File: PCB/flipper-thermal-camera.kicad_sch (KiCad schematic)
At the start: 9 parts, among them J1 Conn_01x08, J2 Conn_01x10, U1 MLX90640ESF-BAB-000-SP, U2 XC6206PxxxMR

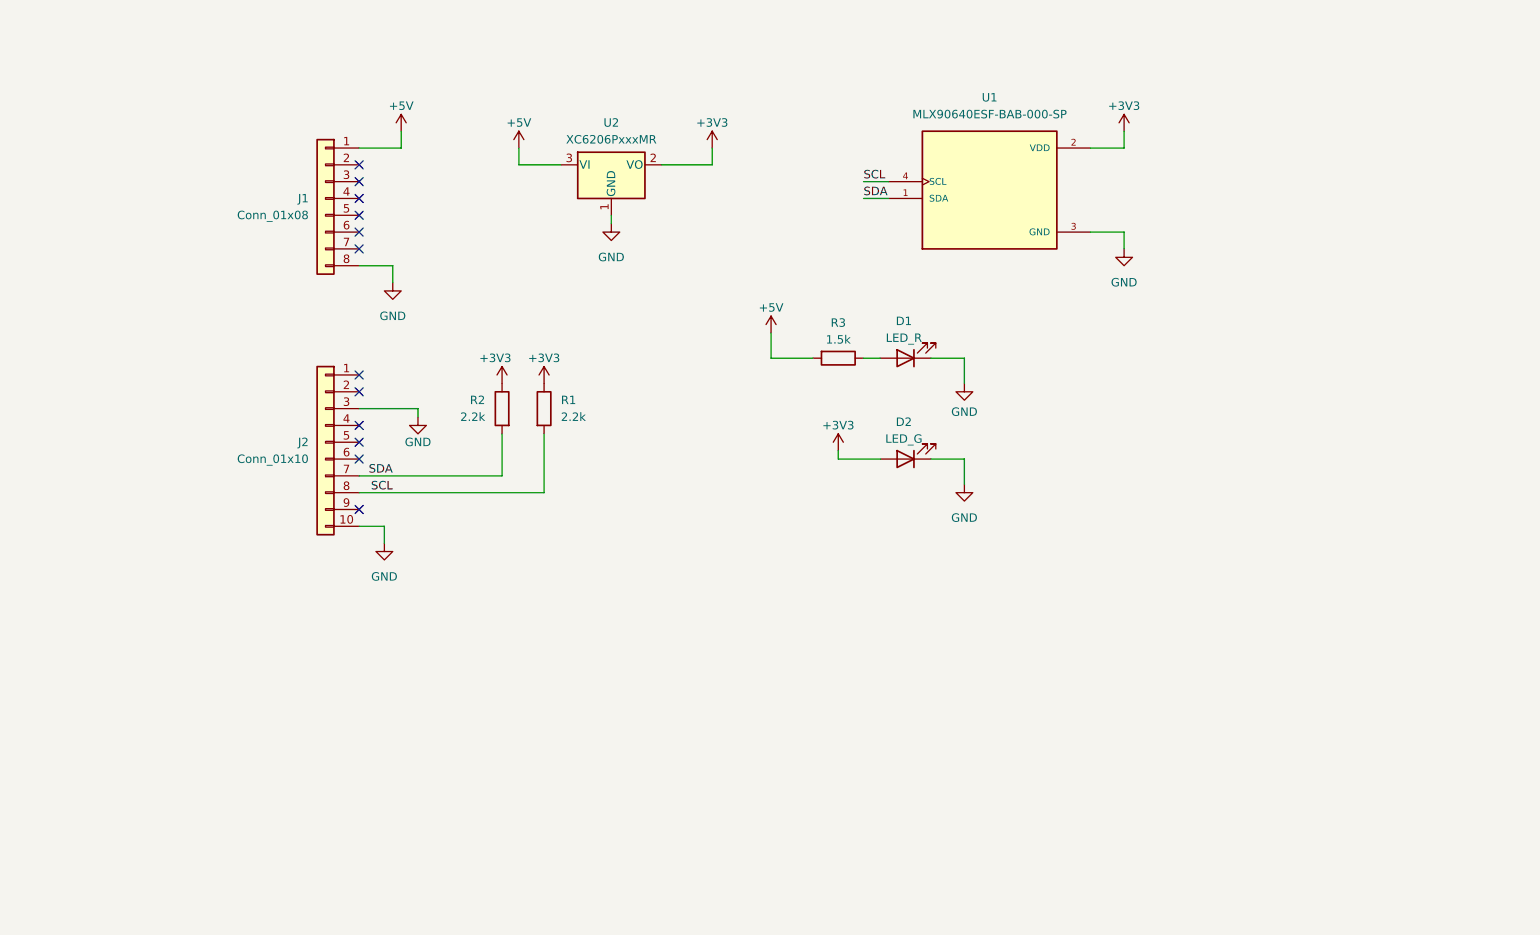
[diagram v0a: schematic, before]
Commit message: add IMU, temp sensor, and light sensor + capacitors
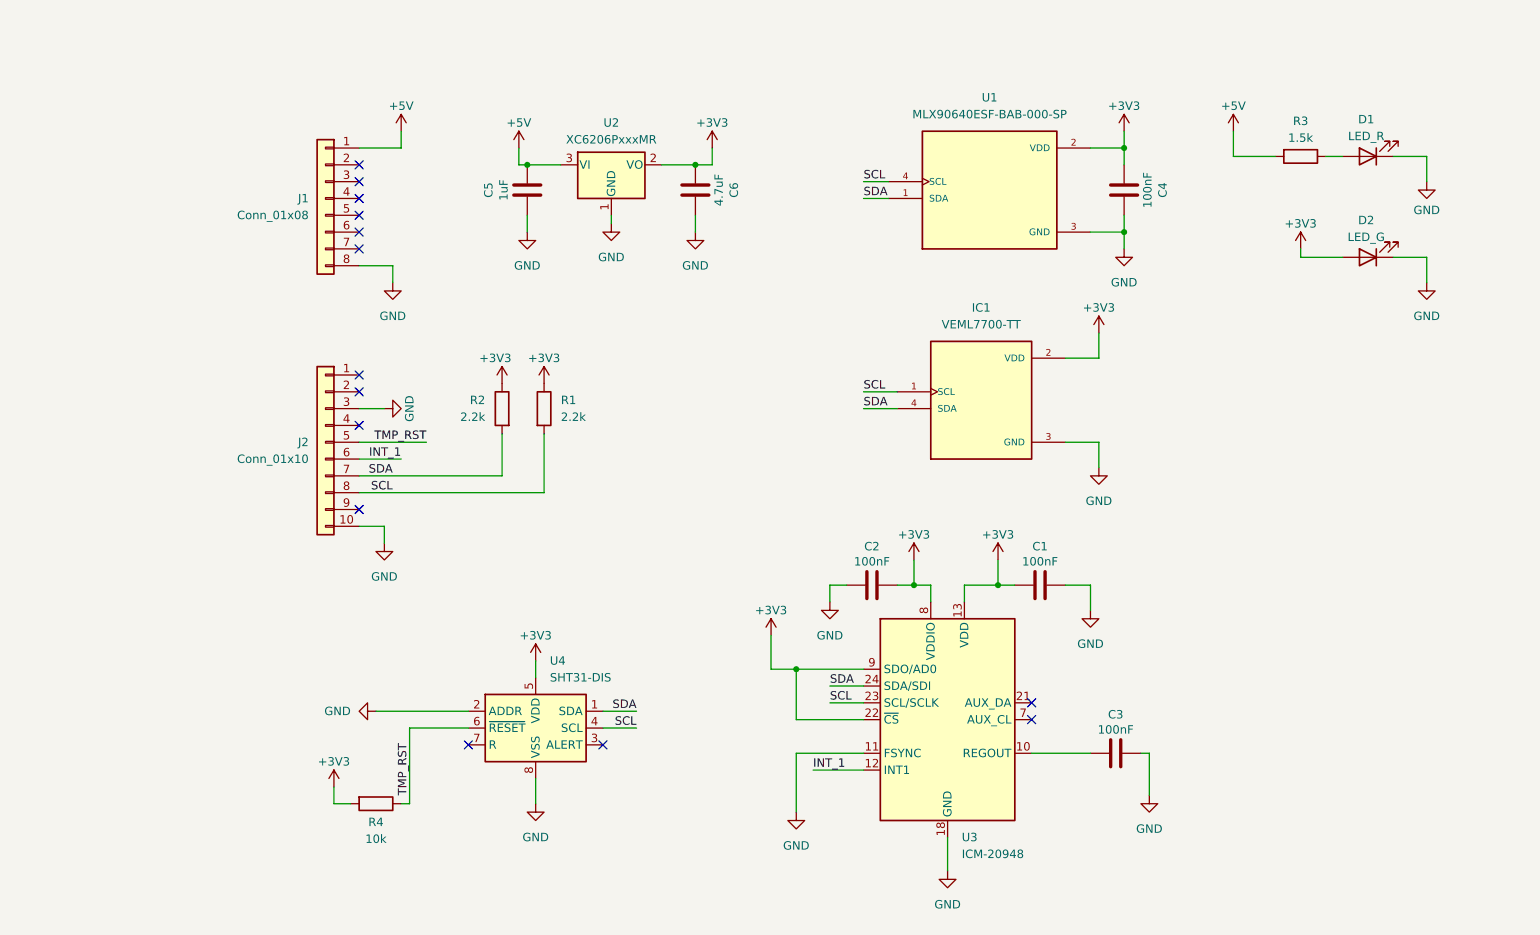
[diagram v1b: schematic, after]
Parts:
- added C1, C2, C3, C4: 100nF, Capacitor_SMD:C_0805_2012Metric, symbol Device:C
- added C5: 1uF, Capacitor_SMD:C_0805_2012Metric, symbol Device:C
- added C6: 4.7uF, Capacitor_SMD:C_0805_2012Metric, symbol Device:C
- added IC1: VEML7700-TT, Components:XDCR_VEML7700-TT, symbol VEML7700-TT:VEML7700-TT
- added R4: 10k, Resistor_SMD:R_0805_2012Metric, symbol Device:R
- added U3: ICM-20948, Sensor_Motion:InvenSense_QFN-24_3x3mm_P0.4mm, symbol Sensor_Motion:ICM-20948
- added U4: SHT31-DIS, Sensor_Humidity:Sensirion_DFN-8-1EP_2.5x2.5mm_P0.5mm_EP1.1x1.7mm, symbol Sensor_Humidity:SHT31-DIS
- D1, D2: footprint (none) -> LED_SMD:LED_0805_2012Metric
- J1: footprint (none) -> Connector_PinHeader_2.54mm:PinHeader_1x08_P2.54mm_Vertical
- J2: footprint (none) -> Connector_PinHeader_2.54mm:PinHeader_1x10_P2.54mm_Vertical
- R1, R2, R3: footprint (none) -> Resistor_SMD:R_0805_2012Metric
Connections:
- net +3V3: now also C1.1, C2.2, C4.1, C6.2, IC1.2 (VDD), R4.2, U3.13 (VDD), U3.22 (~{CS}), U3.8 (VDDIO), U3.9 (SDO/AD0), U4.5 (VDD)
- net +5V: now also C5.2
- net GND: now also C1.2, C2.1, C3.2, C4.2, C5.1, C6.1, IC1.3 (GND), U3.11 (FSYNC), U3.18 (GND), U3.20 (GND), U4.2 (ADDR), U4.8 (VSS), U4.9 (VSS)
- net SCL: now also IC1.1 (SCL), U3.23 (SCL/SCLK), U4.4 (SCL)
- net SDA: now also IC1.4 (SDA), U3.24 (SDA/SDI), U4.1 (SDA)
- net TMP_RST: now reaches J2.5 (Pin_5)
- net TMP_RST: now also R4.1, U4.6 (~{RESET})
- net INT_1: now reaches J2.6 (Pin_6)
- net INT_1: now also U3.12 (INT1)
- new net: C3.1, U3.10 (REGOUT)
- no-connect marks 12 -> 14
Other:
- moved on the sheet: D1, D2, R3

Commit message: finish schematic
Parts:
- J1: footprint Connector_PinHeader_2.54mm:PinHeader_1x08_P2.54mm_Vertical -> Connector_PinHeader_2.54mm:PinHeader_1x08_P2.54mm_Horizontal
- J2: footprint Connector_PinHeader_2.54mm:PinHeader_1x10_P2.54mm_Vertical -> Connector_PinHeader_2.54mm:PinHeader_1x10_P2.54mm_Horizontal
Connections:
- net +5V: now also J1.8 (Pin_8); no longer J1.1 (Pin_1)
- net GND: now also J1.1 (Pin_1), J2.1 (Pin_1), J2.8 (Pin_8); no longer J1.8 (Pin_8), J2.10 (Pin_10), J2.3 (Pin_3)
- net INT_1: now also J2.5 (Pin_5); no longer J2.6 (Pin_6)
- net SCL: now also J2.3 (Pin_3); no longer J2.8 (Pin_8)
- net SDA: now also J2.4 (Pin_4); no longer J2.7 (Pin_7)
- net TMP_RST: now also J2.6 (Pin_6); no longer J2.5 (Pin_5)
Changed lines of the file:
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@@
 	)
 	(symbol
-		(lib_id "Connector_Generic:Conn_01x08")
-		(at 62.23 48.26 0)
-		(mirror y)
-		(unit 1)
-		(body_style 1)
-		(exclude_from_sim no)
-		(in_bom yes)
-		(on_board yes)
-		(in_pos_files yes)
-		(dnp no)
-		(fields_autoplaced yes)
-		(property "Reference" "J1"
-			(at 59.69 48.2599 0)
-			(show_name no)
-			(do_not_autoplace no)
-			(effects
-				(font
-					(size 1.27 1.27)
-				)
-				(justify left)
-			)
-		)
-		(property "Value" "Conn_01x08"
-			(at 59.69 50.7999 0)
-			(show_name no)
-			(do_not_autoplace no)
-			(effects
-				(font
-					(size 1.27 1.27)
-				)
-				(justify left)
-			)
-		)
-		(property "Footprint" "Connector_PinHeader_2.54mm:PinHeader_1x08_P2.54mm_Vertical"
-			(at 62.23 48.26 0)
-			(hide yes)
-			(show_name no)
-			(do_not_autoplace no)
-			(effects
-				(font
-					(size 1.27 1.27)
-				)
-			)
-		)
-		(property "Datasheet" ""
-			(at 62.23 48.26 0)
-			(hide yes)
-			(show_name no)
-			(do_not_autoplace no)
-			(effects
-				(font
-					(size 1.27 1.27)
-				)
-			)
-		)
-		(property "Description" "Generic connector, single row, 01x08, script generated (kicad-library-utils/schlib/autogen/connector/)"
-			(at 62.23 48.26 0)
-			(hide yes)
-			(show_name no)
-			(do_not_autoplace no)
-			(effects
-				(font
-					(size 1.27 1.27)
-				)
-			)
-		)
-		(pin "1"
-		)
-		(pin "3"
-		)
-		(pin "4"
-		)
-		(pin "5"
-		)
-		(pin "6"
-		)
-		(pin "8"
-		)
-		(pin "2"
-		)
-		(pin "7"
-		)
-		(instances
-			(project "flipper-thermal-camera"
-				(path "/20fef62b-baec-4471-9252-b8b8b3debd81"
-					(reference "J1")
-					(unit 1)
-				)
-			)
-		)
-	)
-	(symbol
 		(lib_id "Regulator_Linear:XC6206PxxxMR")
 		(at 105.41 43.18 0)
@@
 	)
 	(symbol
+		(lib_id "Connector_Generic:Conn_01x10")
+		(at 62.23 87.63 180)
+		(unit 1)
+		(body_style 1)
+		(exclude_from_sim no)
+		(in_bom yes)
+		(on_board yes)
+		(in_pos_files yes)
+		(dnp no)
+		(property "Reference" "J2"
+			(at 62.23 68.58 0)
+			(show_name no)
+			(do_not_autoplace no)
+			(effects
+				(font
+					(size 1.27 1.27)
+				)
+			)
+		)
+		(property "Value" "Conn_01x10"
+			(at 62.23 71.12 0)
+			(show_name no)
+			(do_not_autoplace no)
+			(effects
+				(font
+					(size 1.27 1.27)
+				)
+			)
+		)
+		(property "Footprint" "Connector_PinHeader_2.54mm:PinHeader_1x10_P2.54mm_Horizontal"
+			(at 62.23 87.63 0)
+			(hide yes)
+			(show_name no)
+			(do_not_autoplace no)
+			(effects
+				(font
+					(size 1.27 1.27)
+				)
+			)
+		)
+		(property "Datasheet" ""
+			(at 62.23 87.63 0)
+			(hide yes)
+			(show_name no)
+			(do_not_autoplace no)
+			(effects
+				(font
+					(size 1.27 1.27)
+				)
+			)
+		)
+		(property "Description" "Generic connector, single row, 01x10, script generated (kicad-library-utils/schlib/autogen/connector/)"
+			(at 62.23 87.63 0)
+			(hide yes)
+			(show_name no)
+			(do_not_autoplace no)
+			(effects
+				(font
+					(size 1.27 1.27)
+				)
+			)
+		)
+		(pin "9"
+		)
+		(pin "2"
+		)
+		(pin "7"
+		)
+		(pin "10"
+		)
+		(pin "3"
+		)
+		(pin "5"
+		)
+		(pin "4"
+		)
+		(pin "1"
+		)
+		(pin "6"
+		)
+		(pin "8"
+		)
+		(instances
+			(project "flipper-thermal-camera"
+				(path "/20fef62b-baec-4471-9252-b8b8b3debd81"
+					(reference "J2")
+					(unit 1)
+				)
+			)
+		)
+	)
+	(symbol
 		(lib_id "Device:R")
 		(at 69.85 139.7 270)
@@
 	)
 	(symbol
+		(lib_id "Connector_Generic:Conn_01x08")
+		(at 62.23 50.8 180)
+		(unit 1)
+		(body_style 1)
+		(exclude_from_sim no)
+		(in_bom yes)
+		(on_board yes)
+		(in_pos_files yes)
+		(dnp no)
+		(property "Reference" "J1"
+			(at 62.23 34.29 0)
+			(show_name no)
+			(do_not_autoplace no)
+			(effects
+				(font
+					(size 1.27 1.27)
+				)
+			)
+		)
+		(property "Value" "Conn_01x08"
+			(at 62.23 36.83 0)
+			(show_name no)
+			(do_not_autoplace no)
+			(effects
+				(font
+					(size 1.27 1.27)
+				)
+			)
+		)
+		(property "Footprint" "Connector_PinHeader_2.54mm:PinHeader_1x08_P2.54mm_Horizontal"
+			(at 62.23 50.8 0)
+			(hide yes)
+			(show_name no)
+			(do_not_autoplace no)
+			(effects
+				(font
+					(size 1.27 1.27)
+				)
+			)
+		)
+		(property "Datasheet" ""
+			(at 62.23 50.8 0)
+			(hide yes)
+			(show_name no)
+			(do_not_autoplace no)
+			(effects
+				(font
+					(size 1.27 1.27)
+				)
+			)
+		)
+		(property "Description" "Generic connector, single row, 01x08, script generated (kicad-library-utils/schlib/autogen/connector/)"
+			(at 62.23 50.8 0)
+			(hide yes)
+			(show_name no)
+			(do_not_autoplace no)
+			(effects
+				(font
+					(size 1.27 1.27)
+				)
+			)
+		)
+		(pin "1"
+		)
+		(pin "3"
+		)
+		(pin "4"
+		)
+		(pin "5"
+		)
+		(pin "6"
+		)
+		(pin "8"
+		)
+		(pin "2"
+		)
+		(pin "7"
+		)
+		(instances
+			(project "flipper-thermal-camera"
+				(path "/20fef62b-baec-4471-9252-b8b8b3debd81"
+					(reference "J1")
+					(unit 1)
+				)
+			)
+		)
+	)
+	(symbol
 		(lib_id "power:GND")
 		(at 105.41 52.07 0)
@@
 					(unit 1)
 				)
-			)
-		)
-	)
-	(symbol
-		(lib_id "Connector_Generic:Conn_01x10")
-		(at 62.23 85.09 0)
-		(mirror y)
-		(unit 1)
-		(body_style 1)
-		(exclude_from_sim no)
-		(in_bom yes)
-		(on_board yes)
-		(in_pos_files yes)
-		(dnp no)
-		(fields_autoplaced yes)
-		(property "Reference" "J2"
-			(at 59.69 85.0899 0)
-			(show_name no)
-			(do_not_autoplace no)
-			(effects
-				(font
-					(size 1.27 1.27)
-				)
-				(justify left)
-			)
-		)
-		(property "Value" "Conn_01x10"
-			(at 59.69 87.6299 0)
-			(show_name no)
-			(do_not_autoplace no)
-			(effects
-				(font
-					(size 1.27 1.27)
-				)
-				(justify left)
-			)
-		)
-		(property "Footprint" "Connector_PinHeader_2.54mm:PinHeader_1x10_P2.54mm_Vertical"
-			(at 62.23 85.09 0)
-			(hide yes)
-			(show_name no)
-			(do_not_autoplace no)
-			(effects
-				(font
-					(size 1.27 1.27)
-				)
-			)
-		)
-		(property "Datasheet" ""
-			(at 62.23 85.09 0)
-			(hide yes)
-			(show_name no)
-			(do_not_autoplace no)
-			(effects
-				(font
-					(size 1.27 1.27)
-				)
-			)
-		)
-		(property "Description" "Generic connector, single row, 01x10, script generated (kicad-library-utils/schlib/autogen/connector/)"
-			(at 62.23 85.09 0)
-			(hide yes)
-			(show_name no)
-			(do_not_autoplace no)
-			(effects
-				(font
-					(size 1.27 1.27)
-				)
-			)
-		)
-		(pin "9"
-		)
-		(pin "2"
-		)
-		(pin "7"
-		)
-		(pin "10"
-		)
-		(pin "3"
-		)
-		(pin "5"
-		)
-		(pin "4"
-		)
-		(pin "1"
-		)
-		(pin "6"
-		)
-		(pin "8"
-		)
-		(instances
-			(project "flipper-thermal-camera"
-				(path "/20fef62b-baec-4471-9252-b8b8b3debd81"
-					(reference "J2")
-					(unit 1)
-				)

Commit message: finish routing pcb
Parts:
- removed J1: Conn_01x08, Connector_PinHeader_2.54mm:PinHeader_1x08_P2.54mm_Horizontal, symbol Connector_Generic:Conn_01x08
- removed J2: Conn_01x10, Connector_PinHeader_2.54mm:PinHeader_1x10_P2.54mm_Horizontal, symbol Connector_Generic:Conn_01x10
- added A1: Flipper_Zero, Module:Flipper_Zero_Angled, symbol MCU_Module:Flipper_Zero
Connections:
- net +5V: now also A1.1 (5V)
- net GND: now also A1.11 (GND), A1.18 (GND), A1.8 (GND)
- net INT_1: now also A1.14 (USART1.RX)
- net SCL: now also A1.16 (I2C3.SCL)
- net SDA: now also A1.15 (I2C3.SDA)
- net TMP_RST: now also A1.13 (USART1.TX)
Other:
- moved on the sheet: R4, U4

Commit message: add testpoints
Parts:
- added SDA1, TP3, TP4: GND, TestPoint:TestPoint_Pad_D2.0mm, symbol Connector:TestPoint
- added TP1: 3V3, TestPoint:TestPoint_Pad_D2.0mm, symbol Connector:TestPoint
- added TP2: 5V, TestPoint:TestPoint_Pad_D2.0mm, symbol Connector:TestPoint
- added TP5: SCL, TestPoint:TestPoint_Pad_D2.0mm, symbol Connector:TestPoint
- added TP6: TMP_SENS_RST, TestPoint:TestPoint_Pad_D2.0mm, symbol Connector:TestPoint
- added TP7: INT_ICM, TestPoint:TestPoint_Pad_D2.0mm, symbol Connector:TestPoint
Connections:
- net +3V3: now also TP1.1
- net +5V: now also TP2.1
- net GND: now also TP3.1, TP4.1
- net INT_1: now also TP7.1
- net SCL: now also TP5.1
- net SDA: now also SDA1.1
- net TMP_RST: now also TP6.1

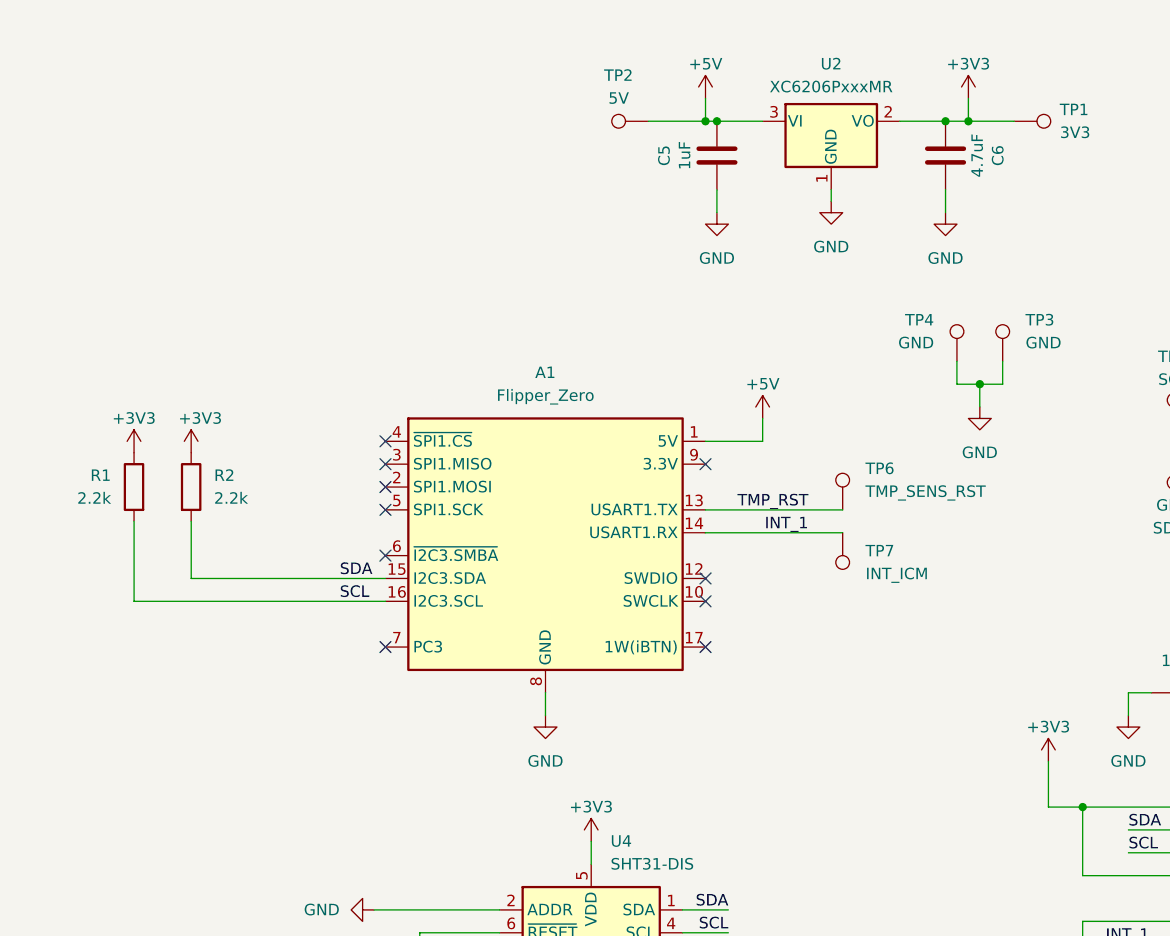
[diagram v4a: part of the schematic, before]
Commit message: add bom
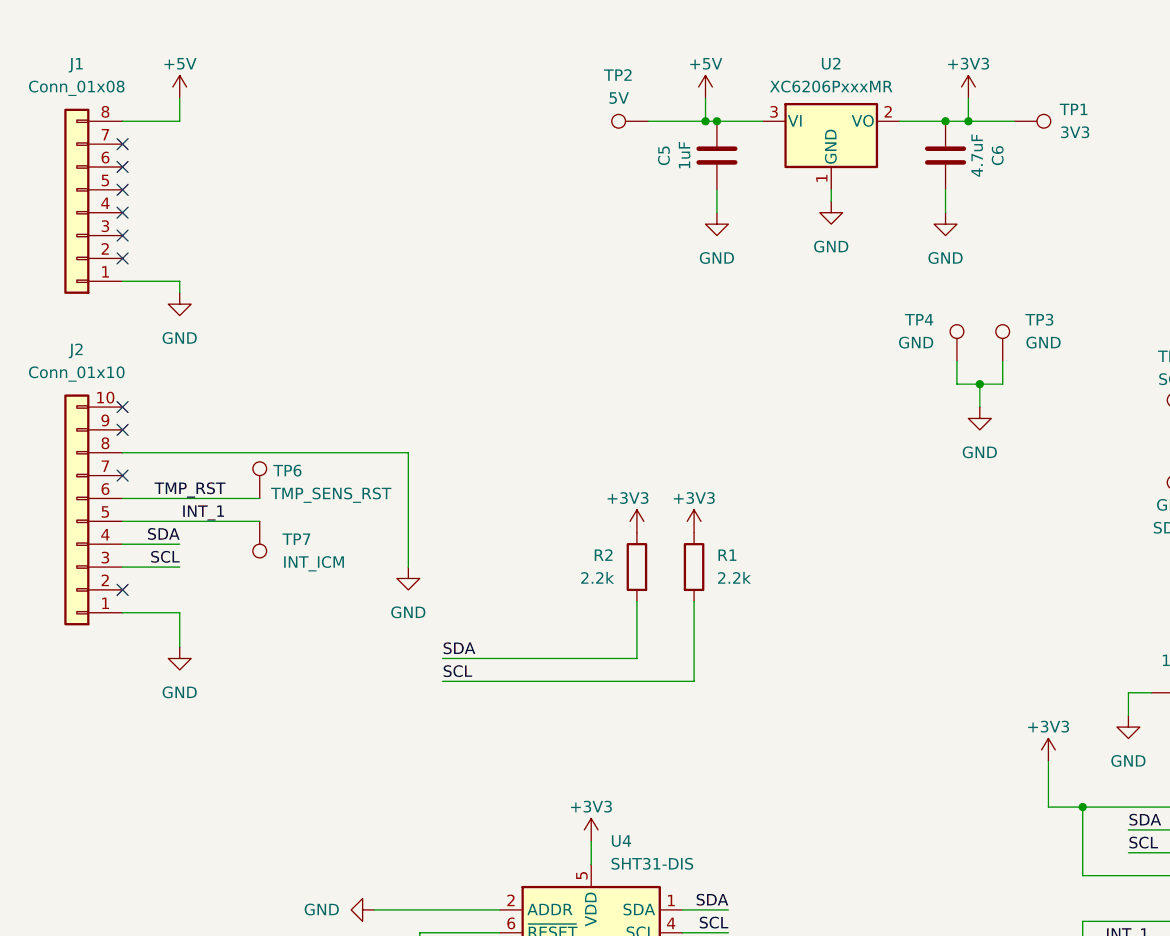
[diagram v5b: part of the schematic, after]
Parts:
- removed A1: Flipper_Zero, Module:Flipper_Zero_Angled, symbol MCU_Module:Flipper_Zero
- added J1: Conn_01x08, Connector_PinHeader_2.54mm:PinHeader_1x08_P2.54mm_Horizontal, symbol Connector_Generic:Conn_01x08
- added J2: Conn_01x10, Connector_PinHeader_2.54mm:PinHeader_1x10_P2.54mm_Horizontal, symbol Connector_Generic:Conn_01x10
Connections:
- net +5V: now also J1.8 (Pin_8)
- net GND: now also J1.1 (Pin_1), J2.1 (Pin_1), J2.8 (Pin_8)
- net INT_1: now also J2.5 (Pin_5)
- net SCL: now also J2.3 (Pin_3)
- net SDA: now also J2.4 (Pin_4)
- net TMP_RST: now also J2.6 (Pin_6)
